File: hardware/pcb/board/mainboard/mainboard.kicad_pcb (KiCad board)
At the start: 6 copper layers, 72.5 x 55 mm, 137 parts, among them J1 Conn_Coaxial, J10 USB_C_Receptacle, J11 2908-05WB-MG, J3 Conn_02x35_Odd_Even_MountingP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, J4 Conn_02x40_Odd_Even_MountingP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, J5 Conn_02x40_Odd_Even_MountingP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, J6 USB_C_Receptacle, J7 Conn_01x30, J8 Conn_01x30, J9 Conn_01x30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

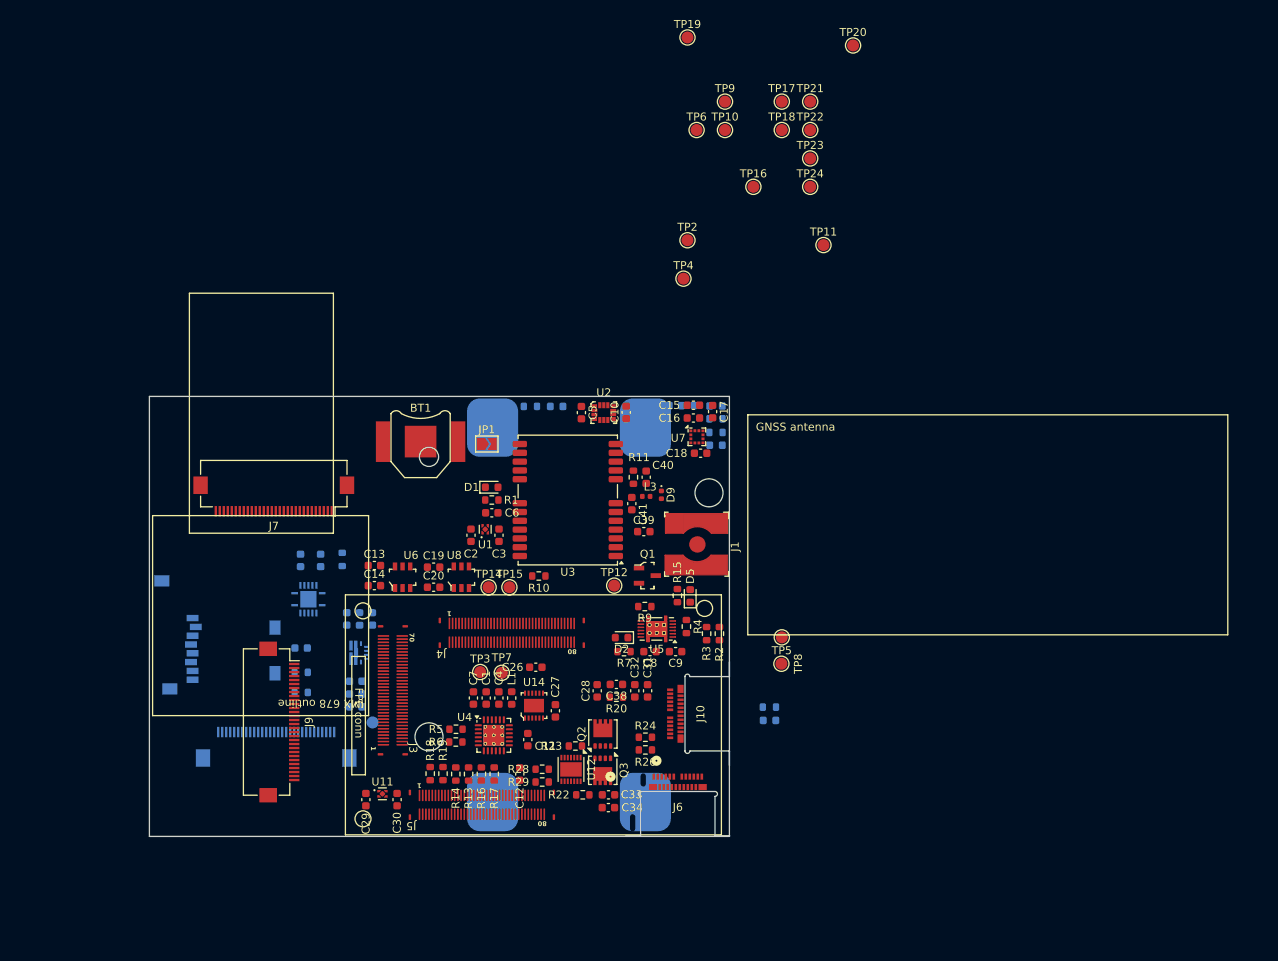
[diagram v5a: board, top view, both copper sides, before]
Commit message: update to KiCad v10.0
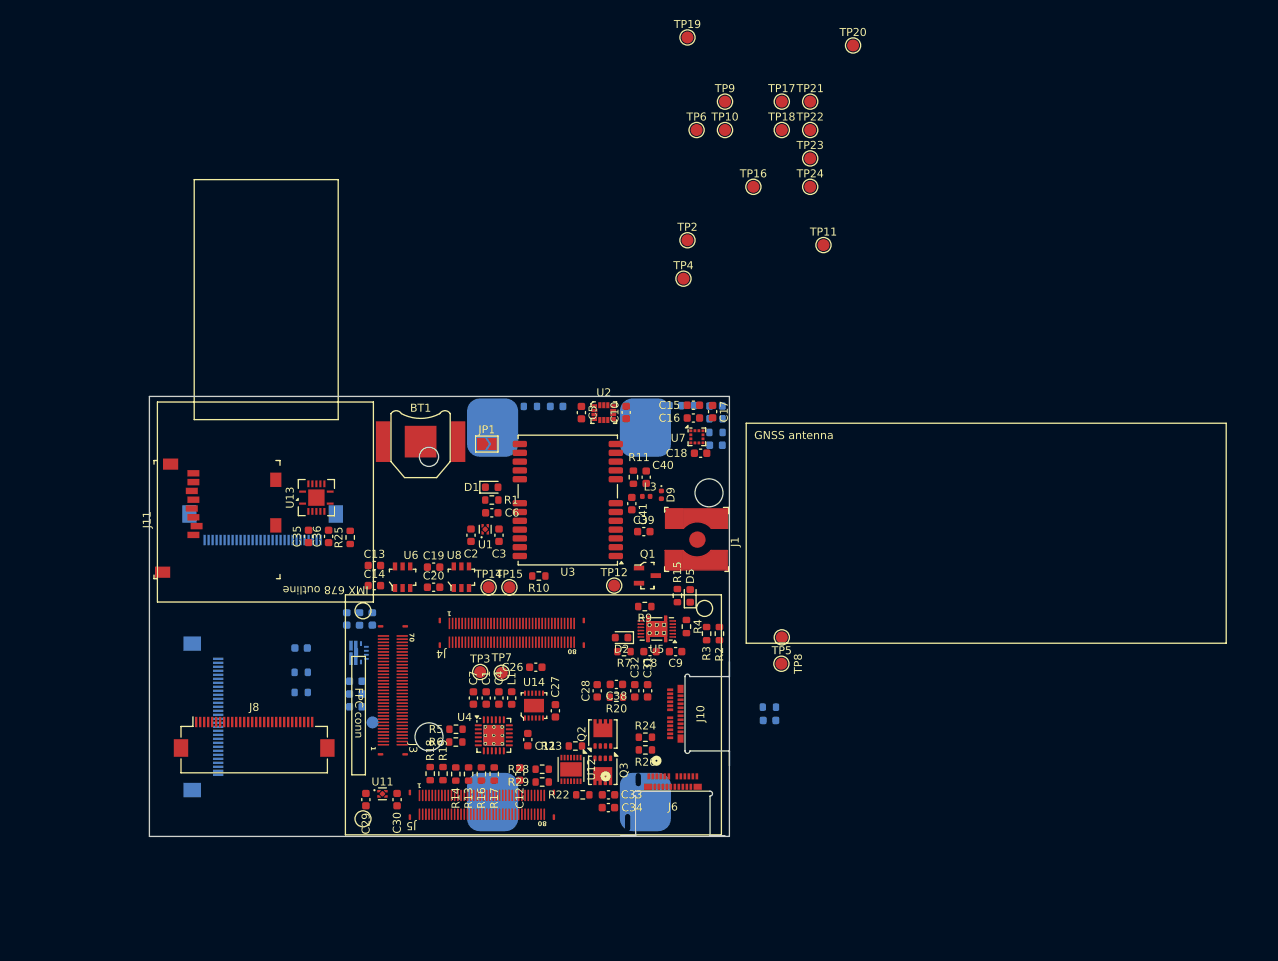
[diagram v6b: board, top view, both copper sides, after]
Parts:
- C35, C36, J11, J8, R25, U13: moved to F.Cu
- J7, J9: moved to B.Cu
- moved U13 12.7 mm to (120.9, 112.7), turned to 90 degrees
- moved J11 10.4 mm to (105.5, 117.3), turned to 90 degrees
- moved J9 9.52 mm to (106.8, 140.1), turned to 90 degrees
- moved J7 3.86 mm to (114.2, 116.1), turned to 0 degrees
- moved C35 3.16 mm to (119.9, 117.5), turned to 90 degrees
- moved C36 3.16 mm to (122.4, 117.5), turned to 90 degrees
- moved J8 3.02 mm to (113.1, 142.6), turned to 0 degrees
- moved R25 2.93 mm to (125.1, 117.6), turned to 90 degrees
- moved J6 0.62 mm to (165.4, 151.3)
- moved J1 0.60 mm to (168.4, 117.9)

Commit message: switch to vertical USB C receptable for shell
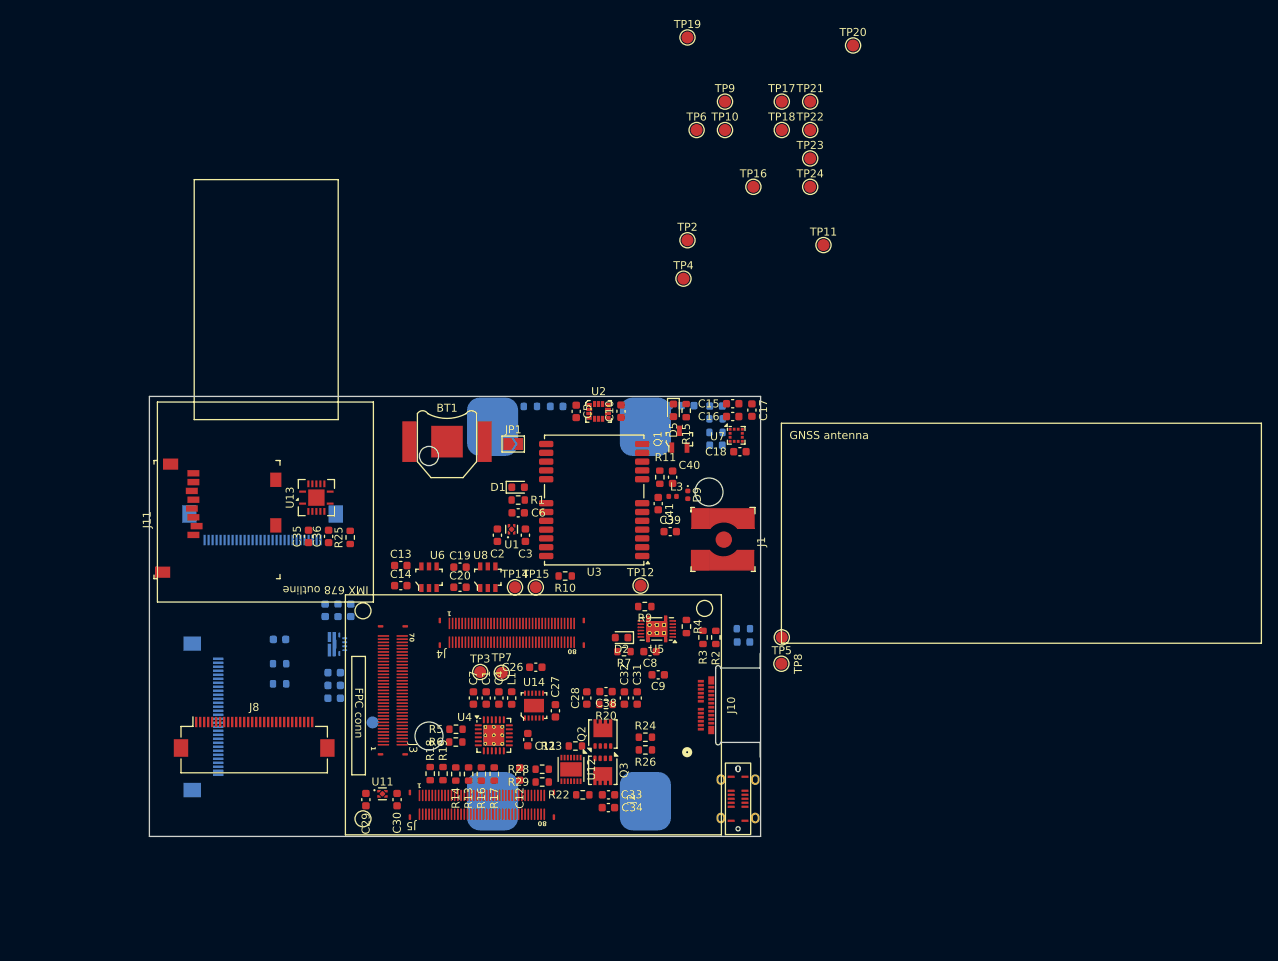
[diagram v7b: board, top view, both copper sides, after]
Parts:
- removed J6: USB_C_Receptacle, Connector_USB:USB_C_CONN_1054550101_MOL
- added J2: USB_C_Receptacle_USB2.0_16P, unsurv_offline_pcb_footprints:2171820001_USB_C_MOLEX, F.Cu at (173.6, 150.3)
- moved D5 23.3 mm to (165.5, 101.7), turned to -90 degrees
- moved R15 23.2 mm to (167.1, 101.8), turned to 90 degrees
- moved Q1 17.5 mm to (166.2, 105.3), turned to 90 degrees
- moved D6 10.3 mm to (174.3, 130.7)
- moved R21 10.3 mm to (174.2, 129.0)
- moved C15 4.92 mm to (172.9, 100.9)
- moved C16 4.92 mm to (172.9, 102.5)
- moved C17 4.92 mm to (175.3, 101.7)
- moved C18 4.92 mm to (173.8, 106.9)
- moved U7 4.92 mm to (173.3, 104.9)
- moved J10 3.98 mm to (172.7, 138.6)
- moved C9 3.63 mm to (163.6, 134.8)
- moved C13 3.30 mm to (131.4, 121.1)
- moved C14 3.30 mm to (131.4, 123.7)
- moved C2 3.30 mm to (143.5, 117.3)
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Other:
- board size 72.5 x 55 mm -> 76.4 x 55 mm

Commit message: length match cam0 pairs
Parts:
- C37, R30, R31: moved to F.Cu
- moved C21 42.7 mm to (84.9, 156.8)
- moved C22 42.7 mm to (84.9, 155.2)
- moved C23 42.7 mm to (84.9, 153.7)
- moved C24 42.7 mm to (83.8, 145.9)
- moved C25 42.7 mm to (87.0, 145.9)
- moved U9 42.7 mm to (85.1, 150.1)
- moved L2 42.7 mm to (85.4, 145.9)
- moved TP13 41.0 mm to (89.7, 155.6)
- moved R31 29.0 mm to (117.9, 107.0), turned to -90 degrees
- moved R30 26.8 mm to (120.4, 107.0), turned to -90 degrees
- moved C37 24.5 mm to (123.4, 107.0), turned to -90 degrees
- moved J9 10.2 mm to (116.9, 139.7)
- moved J7 7.15 mm to (114.0, 123.2)
- moved J8 1.03 mm to (114.0, 142.1)
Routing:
- net CAM0_MClk: track 0.00 -> 25.4 mm, vias 0 -> 2
- net CAM0_MDP3: track 0.00 -> 25.4 mm, vias 0 -> 2
- net CAM0_MDN1: track 0.00 -> 25.4 mm, vias 0 -> 2
- net CAM0_MDP1: track 0.00 -> 25.4 mm, vias 0 -> 2
- net CAM0_MCP: track 0.00 -> 25.4 mm, vias 0 -> 2
- net CAM0_MDN3: track 0.00 -> 25.4 mm, vias 0 -> 2
- net CAM0_MCN: track 0.00 -> 25.3 mm, vias 0 -> 2
- net CAM0_MDP2: track 0.00 -> 25.3 mm, vias 0 -> 2
- net CAM0_MDN0: track 0.00 -> 25.3 mm, vias 0 -> 2
- net CAM0_MDN2: track 0.00 -> 25.3 mm, vias 0 -> 2
- net CAM0_MDP0: track 0.00 -> 25.3 mm, vias 0 -> 2
